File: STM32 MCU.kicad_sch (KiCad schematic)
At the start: 31 parts, among them J4 Conn_01x04_Pin, J5 Conn_01x02_Pin, SW2 SW_Push, SW5 SW_Push, U3 STM32G474RETx, Y1 16MHz

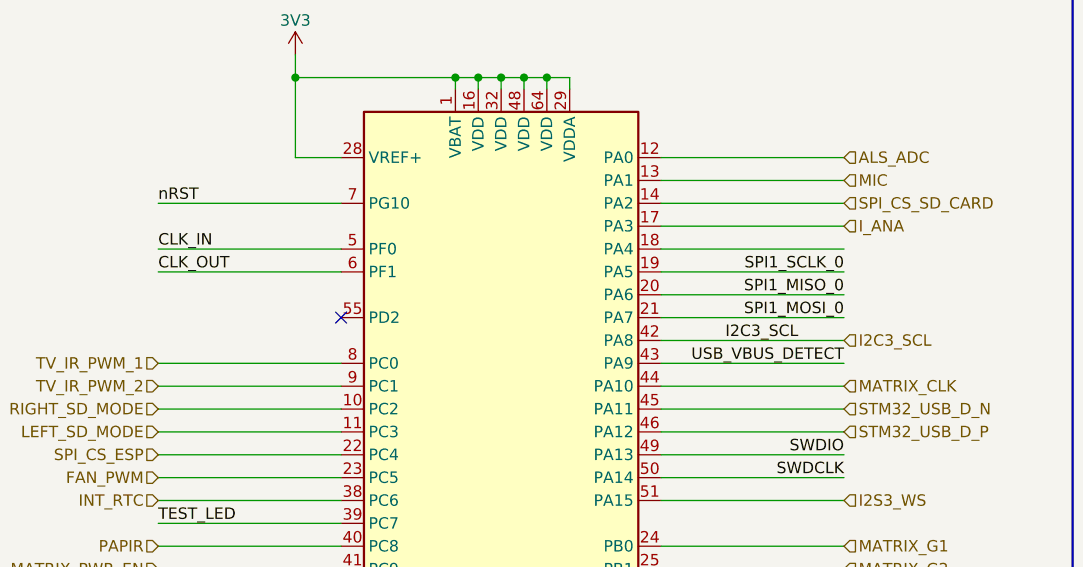
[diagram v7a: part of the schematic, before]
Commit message: finishing pinout to stm from usbcpd
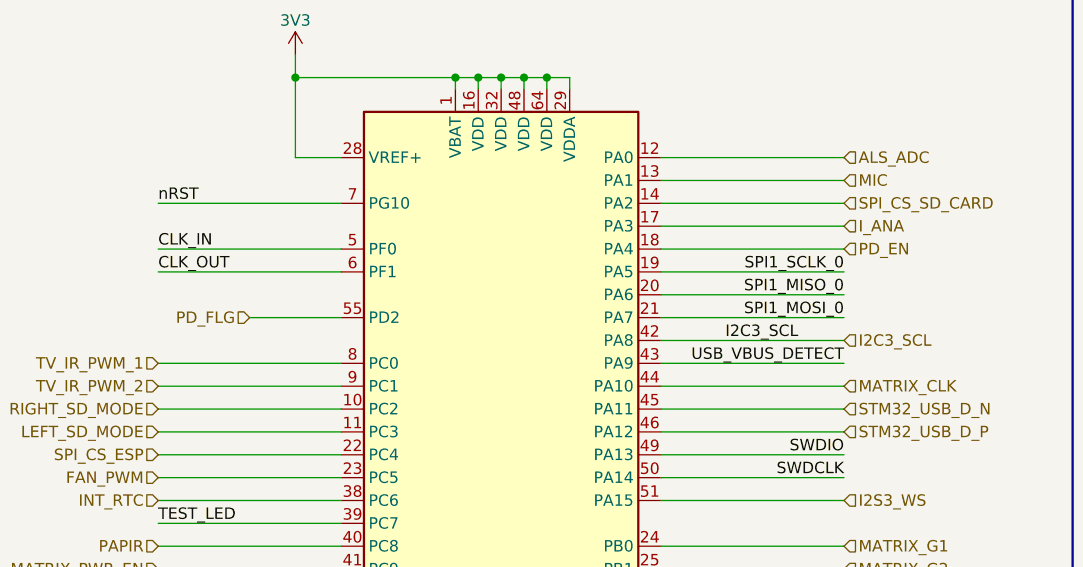
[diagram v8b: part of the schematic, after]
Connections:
- net PD_EN: now reaches U3.18 (PA4)
- net PD_FLG: now reaches U3.55 (PD2)
- no-connect marks 1 -> 0
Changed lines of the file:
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@@
 		(color 0 0 0 0)
 	)
-	(no_connect
-		(at 52.07 54.61)
-	)
 	(wire
 		(pts
@@
 		(pts
 			(xy 165.1 34.29) (xy 165.1 36.83)
+		)
+		(stroke
+			(width 0)
+			(type default)
+		)
+	)
+	(wire
+		(pts
+			(xy 41.91 54.61) (xy 52.07 54.61)
 		)
 		(stroke
@@
 		)
 	)
+	(hierarchical_label "PD_FLG"
+		(shape input)
+		(at 41.91 54.61 180)
+		(effects
+			(font
+				(size 1.27 1.27)
+			)
+			(justify right)
+		)
+	)
 	(hierarchical_label "I2S2_WS"
 		(shape input)
@@
 		)
 	)
+	(hierarchical_label "PD_EN"
+		(shape input)
+		(at 107.95 46.99 0)
+		(effects
+			(font
+				(size 1.27 1.27)
+			)
+			(justify left)
+		)
+	)
